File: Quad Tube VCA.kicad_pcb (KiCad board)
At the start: 2 copper layers, 162.6 x 100.3 mm, 226 parts, among them IC1 TL072, IC10 TL072, IC2 LM358, IC3 TL072, IC4 LM358, IC5 TL072, IC6 LM358, IC7 TL072, IC8 LM358, IC9 TL072

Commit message: updates positions
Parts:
- moved C50 29.5 mm to (226.2, 123.3)
- moved IC8 25.7 mm to (222.5, 118.1)
- moved C49 25.7 mm to (218.7, 113.4)
- moved R80 23.3 mm to (226.4, 113.4)
- moved C45 21.0 mm to (211.5, 118.7)
- moved R79 21.0 mm to (211.5, 116.2)
- moved R76 21.0 mm to (215.1, 121.5)
- moved C44 14.7 mm to (219.1, 123.3)
- moved C47 10.2 mm to (190.1, 120.1)
- moved R75 8.14 mm to (212.6, 124.8)
- moved D16 4.07 mm to (220.3, 71.1), turned to 180 degrees
- moved D12 3.89 mm to (178.3, 71.0), turned to 180 degrees
- moved D8 3.59 mm to (135.9, 71.1), turned to 180 degrees
- moved D4 3.42 mm to (95.2, 70.9), turned to 180 degrees
- moved D3 2.32 mm to (75.3, 70.9)
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
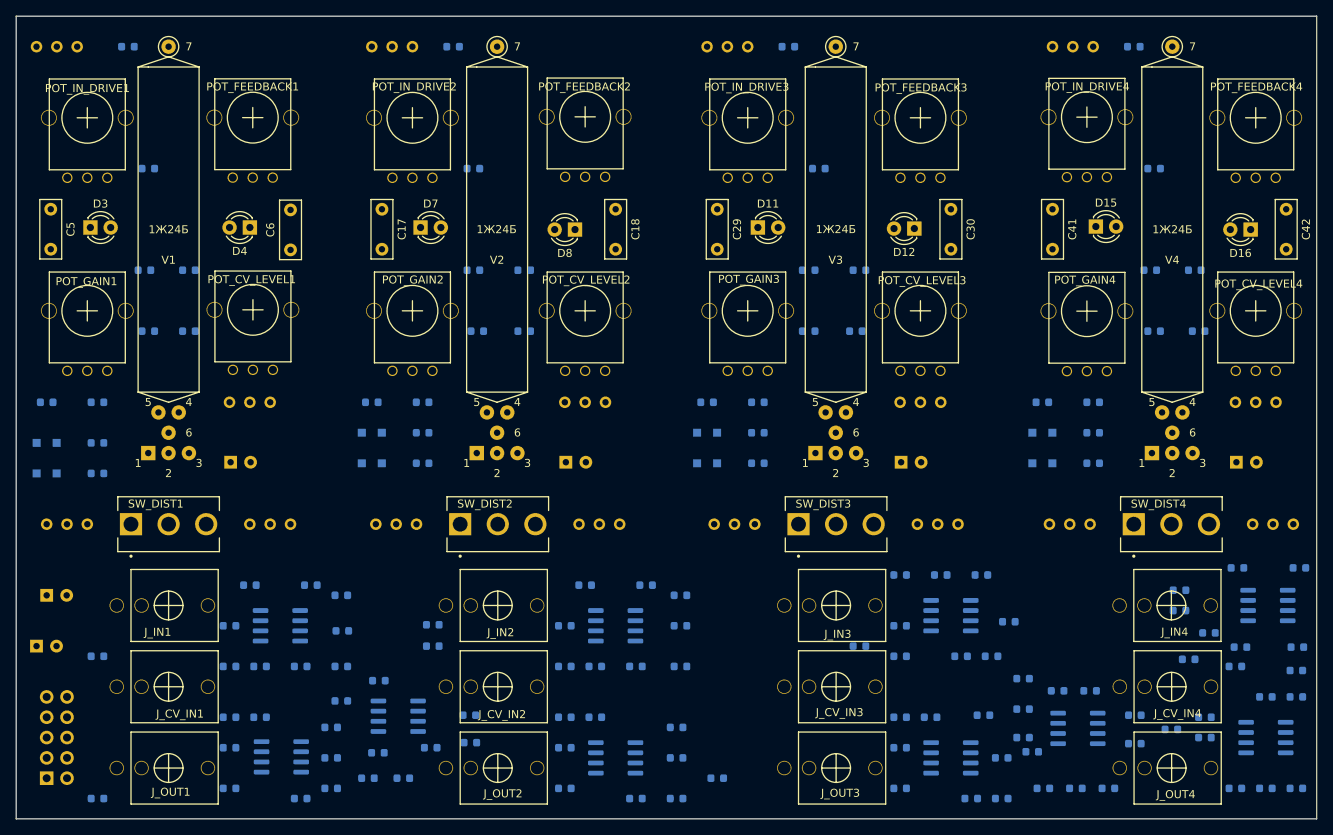
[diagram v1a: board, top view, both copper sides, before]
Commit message: tightens up positions
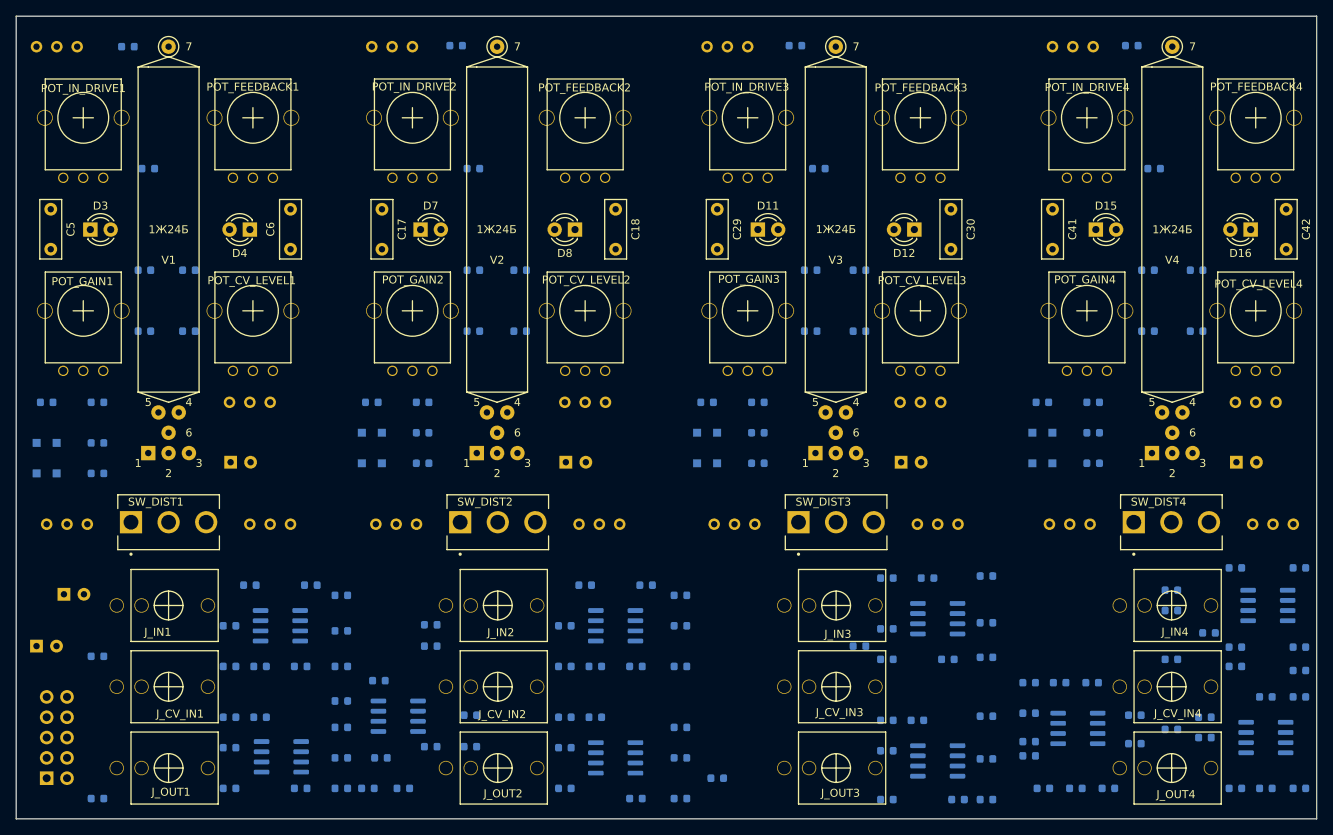
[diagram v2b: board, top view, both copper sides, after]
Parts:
- moved C47 2.80 mm to (187.3, 120.3)
- moved C3 2.16 mm to (72.0, 116.7)
- moved R45 2.16 mm to (174.9, 142.4)
- moved R75 2.16 mm to (210.4, 124.8)
- moved R42 1.91 mm to (187.3, 137.3)
- moved R43 1.91 mm to (187.3, 142.4)
- moved C27 1.69 mm to (174.9, 136.3)
- moved C33 1.69 mm to (174.9, 121.0)
- moved C35 1.69 mm to (182.5, 124.8)
- moved C36 1.69 mm to (178.7, 132.5)
- moved C37 1.69 mm to (174.9, 114.7)
- moved C38 1.69 mm to (180.0, 114.7)
- moved R44 1.69 mm to (174.9, 132.5)
- moved R56 1.69 mm to (174.9, 124.8)
- moved IC5 1.69 mm to (181.2, 137.5)
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
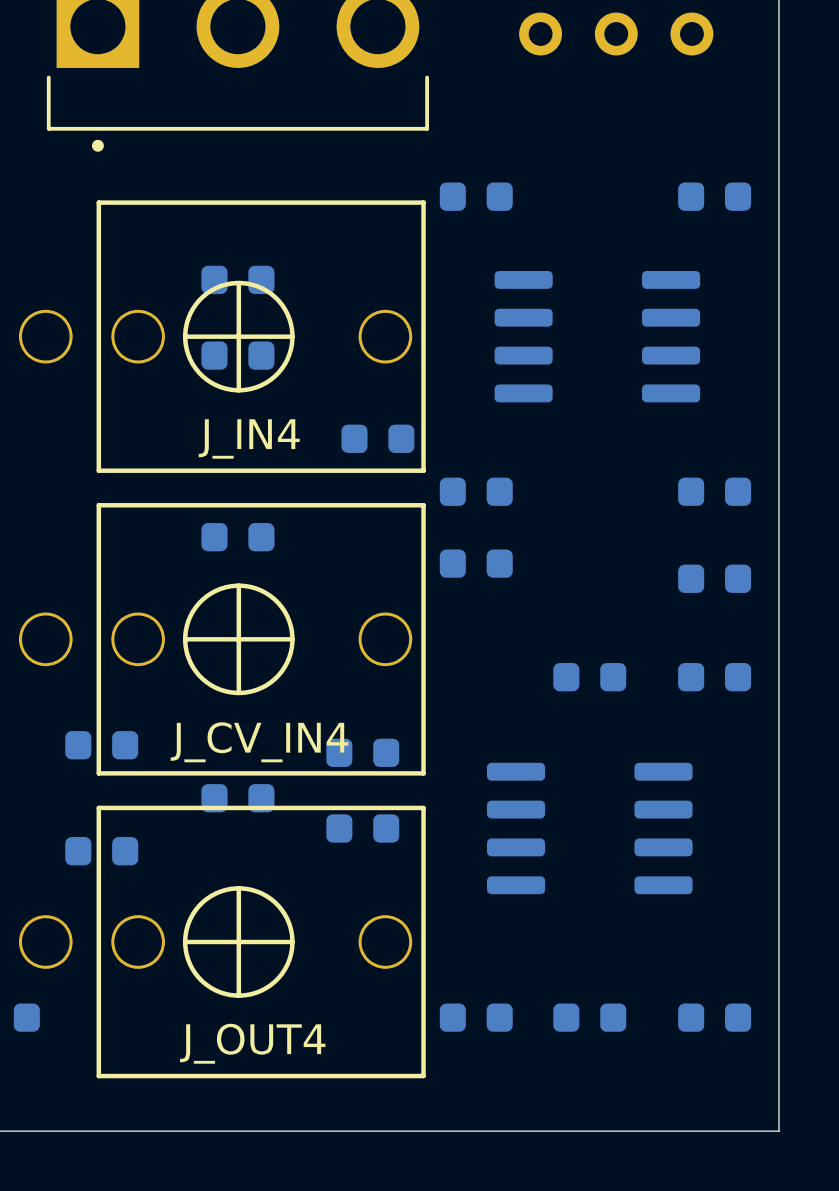
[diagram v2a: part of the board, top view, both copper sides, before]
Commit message: updates footprints in schematic
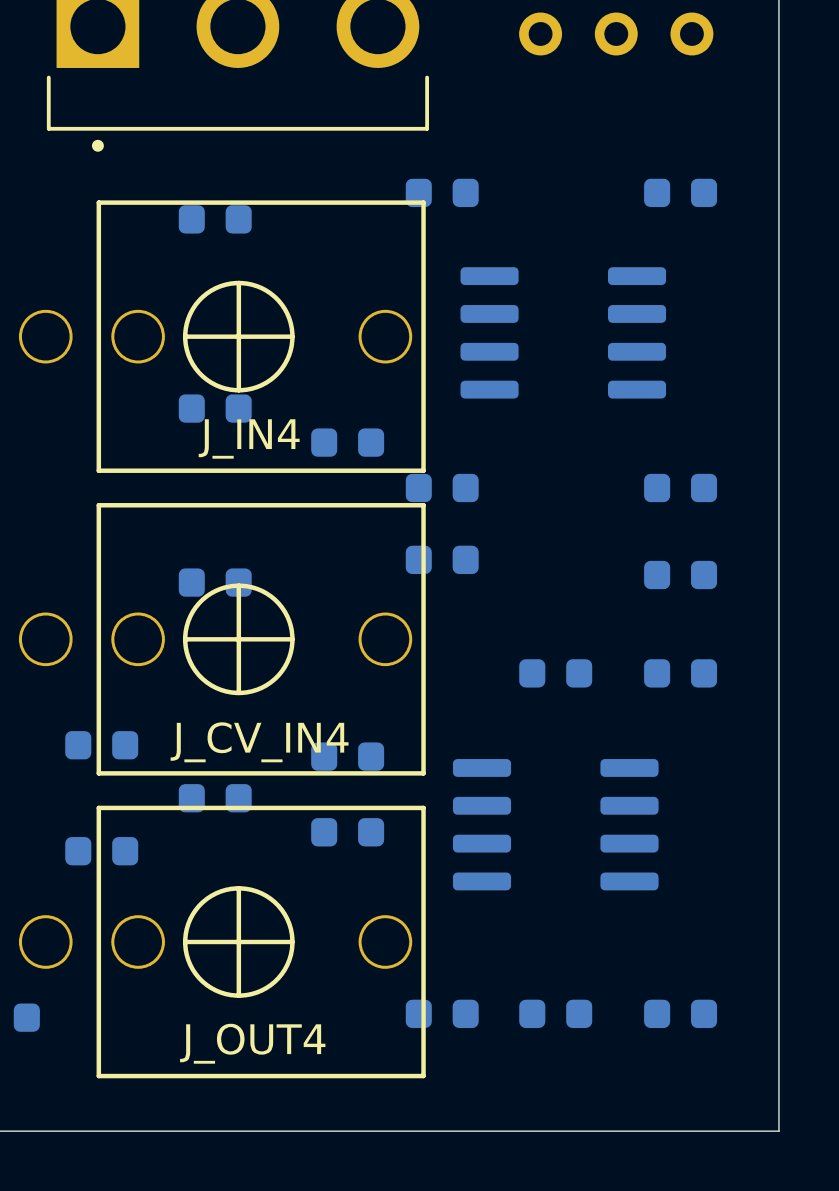
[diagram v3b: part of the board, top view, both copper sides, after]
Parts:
- moved R79 2.17 mm to (209.7, 114.2)
- moved C45 1.93 mm to (209.7, 120.5)
- moved R75 1.70 mm to (209.7, 126.4)
- moved C46 1.15 mm to (221.1, 140.8)
- moved C48 1.15 mm to (217.3, 125.6)
- moved IC7 1.15 mm to (221.1, 134.5)
- moved R63 1.15 mm to (225.3, 140.8)
- moved R65 1.15 mm to (217.3, 140.8)
- moved C44 1.15 mm to (217.3, 123.2)
- moved C49 1.15 mm to (217.3, 113.3)
- moved C50 1.15 mm to (225.3, 123.2)
- moved IC8 1.15 mm to (221.4, 118.0)
- moved R61 1.15 mm to (225.3, 126.1)
- moved R80 1.15 mm to (225.3, 113.3)
- moved C40 1.15 mm to (225.3, 129.4)
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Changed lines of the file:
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@@
   )
   (module Resistor_SMD:R_0603_1608Metric (layer B.Cu)
-    (at 210.439 133.604)
+    (at 209.677 133.604)
     (descr "Resistor SMD 0603 (1608 Metric), square (rectangular) end terminal, IPC_7351 nominal, (Body size source: http://www.tortai-tech.com/upload/download/2011102023233369053.pdf), generated with kicad-footprint-generator")
     (tags resistor)
@@
   )
   (module Resistor_SMD:R_0603_1608Metric (layer B.Cu)
-    (at 226.441 113.411)
+    (at 225.298 113.284)
     (descr "Resistor SMD 0603 (1608 Metric), square (rectangular) end terminal, IPC_7351 nominal, (Body size source: http://www.tortai-tech.com/upload/download/2011102023233369053.pdf), generated with kicad-footprint-generator")
     (tags resistor)
@@
   )
   (module Resistor_SMD:R_0603_1608Metric (layer B.Cu)
-    (at 210.439 116.205)
+    (at 209.677 114.173)
     (descr "Resistor SMD 0603 (1608 Metric), square (rectangular) end terminal, IPC_7351 nominal, (Body size source: http://www.tortai-tech.com/upload/download/2011102023233369053.pdf), generated with kicad-footprint-generator")
     (tags resistor)
@@
   )
   (module Resistor_SMD:R_0603_1608Metric (layer B.Cu)
-    (at 215.138 121.539 180)
+    (at 214.122 121.666 180)
     (descr "Resistor SMD 0603 (1608 Metric), square (rectangular) end terminal, IPC_7351 nominal, (Body size source: http://www.tortai-tech.com/upload/download/2011102023233369053.pdf), generated with kicad-footprint-generator")
     (tags resistor)
@@
   )
   (module Resistor_SMD:R_0603_1608Metric (layer B.Cu)
-    (at 210.439 124.841 180)
+    (at 209.677 126.365 180)
     (descr "Resistor SMD 0603 (1608 Metric), square (rectangular) end terminal, IPC_7351 nominal, (Body size source: http://www.tortai-tech.com/upload/download/2011102023233369053.pdf), generated with kicad-footprint-generator")
     (tags resistor)
@@
   )
   (module Resistor_SMD:R_0603_1608Metric (layer B.Cu)
-    (at 218.44 140.97)
+    (at 217.297 140.843)
     (descr "Resistor SMD 0603 (1608 Metric), square (rectangular) end terminal, IPC_7351 nominal, (Body size source: http://www.tortai-tech.com/upload/download/2011102023233369053.pdf), generated with kicad-footprint-generator")
     (tags resistor)
@@
   )
   (module Resistor_SMD:R_0603_1608Metric (layer B.Cu)
-    (at 214.63 132.08 180)
+    (at 214.122 132.207 180)
     (descr "Resistor SMD 0603 (1608 Metric), square (rectangular) end terminal, IPC_7351 nominal, (Body size source: http://www.tortai-tech.com/upload/download/2011102023233369053.pdf), generated with kicad-footprint-generator")
     (tags resistor)
@@
   )
   (module Resistor_SMD:R_0603_1608Metric (layer B.Cu)
-    (at 226.441 140.97 180)
+    (at 225.298 140.843 180)
     (descr "Resistor SMD 0603 (1608 Metric), square (rectangular) end terminal, IPC_7351 nominal, (Body size source: http://www.tortai-tech.com/upload/download/2011102023233369053.pdf), generated with kicad-footprint-generator")
     (tags resistor)
@@
   )
   (module Resistor_SMD:R_0603_1608Metric (layer B.Cu)
-    (at 222.25 129.54)
+    (at 221.107 129.413)
     (descr "Resistor SMD 0603 (1608 Metric), square (rectangular) end terminal, IPC_7351 nominal, (Body size source: http://www.tortai-tech.com/upload/download/2011102023233369053.pdf), generated with kicad-footprint-generator")
     (tags resistor)
@@
   )
   (module Resistor_SMD:R_0603_1608Metric (layer B.Cu)
-    (at 226.441 126.238)
+    (at 225.298 126.111)
     (descr "Resistor SMD 0603 (1608 Metric), square (rectangular) end terminal, IPC_7351 nominal, (Body size source: http://www.tortai-tech.com/upload/download/2011102023233369053.pdf), generated with kicad-footprint-generator")
     (tags resistor)
@@
   )
   (module Package_SO:SOIC-8_3.9x4.9mm_P1.27mm (layer B.Cu)
-    (at 222.504 118.11)
+    (at 221.361 117.983)
     (descr "SOIC, 8 Pin (JEDEC MS-012AA, https://www.analog.com/media/en/package-pcb-resources/package/pkg_pdf/soic_narrow-r/r_8.pdf), generated with kicad-footprint-generator ipc_gullwing_generator.py")
     (tags "SOIC SO")
@@
   )
   (module Package_SO:SOIC-8_3.9x4.9mm_P1.27mm (layer B.Cu)
-    (at 222.25 134.62)
+    (at 221.107 134.493)
     (descr "SOIC, 8 Pin (JEDEC MS-012AA, https://www.analog.com/media/en/package-pcb-resources/package/pkg_pdf/soic_narrow-r/r_8.pdf), generated with kicad-footprint-generator ipc_gullwing_generator.py")
     (tags "SOIC SO")
@@
   )
   (module Capacitor_SMD:C_0603_1608Metric (layer B.Cu)
-    (at 226.441 123.317 180)
+    (at 225.298 123.19 180)
     (descr "Capacitor SMD 0603 (1608 Metric), square (rectangular) end terminal, IPC_7351 nominal, (Body size source: http://www.tortai-tech.com/upload/download/2011102023233369053.pdf), generated with kicad-footprint-generator")
     (tags capacitor)
@@
   )
   (module Capacitor_SMD:C_0603_1608Metric (layer B.Cu)
-    (at 218.44 113.411)
+    (at 217.297 113.284)
     (descr "Capacitor SMD 0603 (1608 Metric), square (rectangular) end terminal, IPC_7351 nominal, (Body size source: http://www.tortai-tech.com/upload/download/2011102023233369053.pdf), generated with kicad-footprint-generator")
     (tags capacitor)
@@
   )
   (module Capacitor_SMD:C_0603_1608Metric (layer B.Cu)
-    (at 218.44 125.73)
+    (at 217.297 125.603)
     (descr "Capacitor SMD 0603 (1608 Metric), square (rectangular) end terminal, IPC_7351 nominal, (Body size source: http://www.tortai-tech.com/upload/download/2011102023233369053.pdf), generated with kicad-footprint-generator")
     (tags capacitor)
@@
   )
   (module Capacitor_SMD:C_0603_1608Metric (layer B.Cu)
-    (at 222.25 140.97)
+    (at 221.107 140.843)
     (descr "Capacitor SMD 0603 (1608 Metric), square (rectangular) end terminal, IPC_7351 nominal, (Body size source: http://www.tortai-tech.com/upload/download/2011102023233369053.pdf), generated with kicad-footprint-generator")
     (tags capacitor)
@@
   )
   (module Capacitor_SMD:C_0603_1608Metric (layer B.Cu)
-    (at 210.439 118.745 180)
+    (at 209.677 120.523 180)
     (descr "Capacitor SMD 0603 (1608 Metric), square (rectangular) end terminal, IPC_7351 nominal, (Body size source: http://www.tortai-tech.com/upload/download/2011102023233369053.pdf), generated with kicad-footprint-generator")
     (tags capacitor)
@@
   )
   (module Capacitor_SMD:C_0603_1608Metric (layer B.Cu)
-    (at 218.44 123.317 180)
+    (at 217.297 123.19 180)
     (descr "Capacitor SMD 0603 (1608 Metric), square (rectangular) end terminal, IPC_7351 nominal, (Body size source: http://www.tortai-tech.com/upload/download/2011102023233369053.pdf), generated with kicad-footprint-generator")
     (tags capacitor)
@@
   )
   (module Capacitor_SMD:C_0603_1608Metric (layer B.Cu)
-    (at 226.441 129.54 180)
+    (at 225.298 129.413 180)
     (descr "Capacitor SMD 0603 (1608 Metric), square (rectangular) end terminal, IPC_7351 nominal, (Body size source: http://www.tortai-tech.com/upload/download/2011102023233369053.pdf), generated with kicad-footprint-generator")
     (tags capacitor)
@@
   )
   (module Capacitor_SMD:C_0603_1608Metric (layer B.Cu)
-    (at 214.63 134.62)
+    (at 214.122 134.747)
     (descr "Capacitor SMD 0603 (1608 Metric), square (rectangular) end terminal, IPC_7351 nominal, (Body size source: http://www.tortai-tech.com/upload/download/2011102023233369053.pdf), generated with kicad-footprint-generator")
     (tags capacitor)
